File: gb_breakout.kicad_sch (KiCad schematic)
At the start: 19 parts, among them IC1 74ALVC164245DGG_11, IC2 74ALVC164245DGG_11, J1 Conn_02x16_Counter_Clockwise, U1 Cartridge_Bus

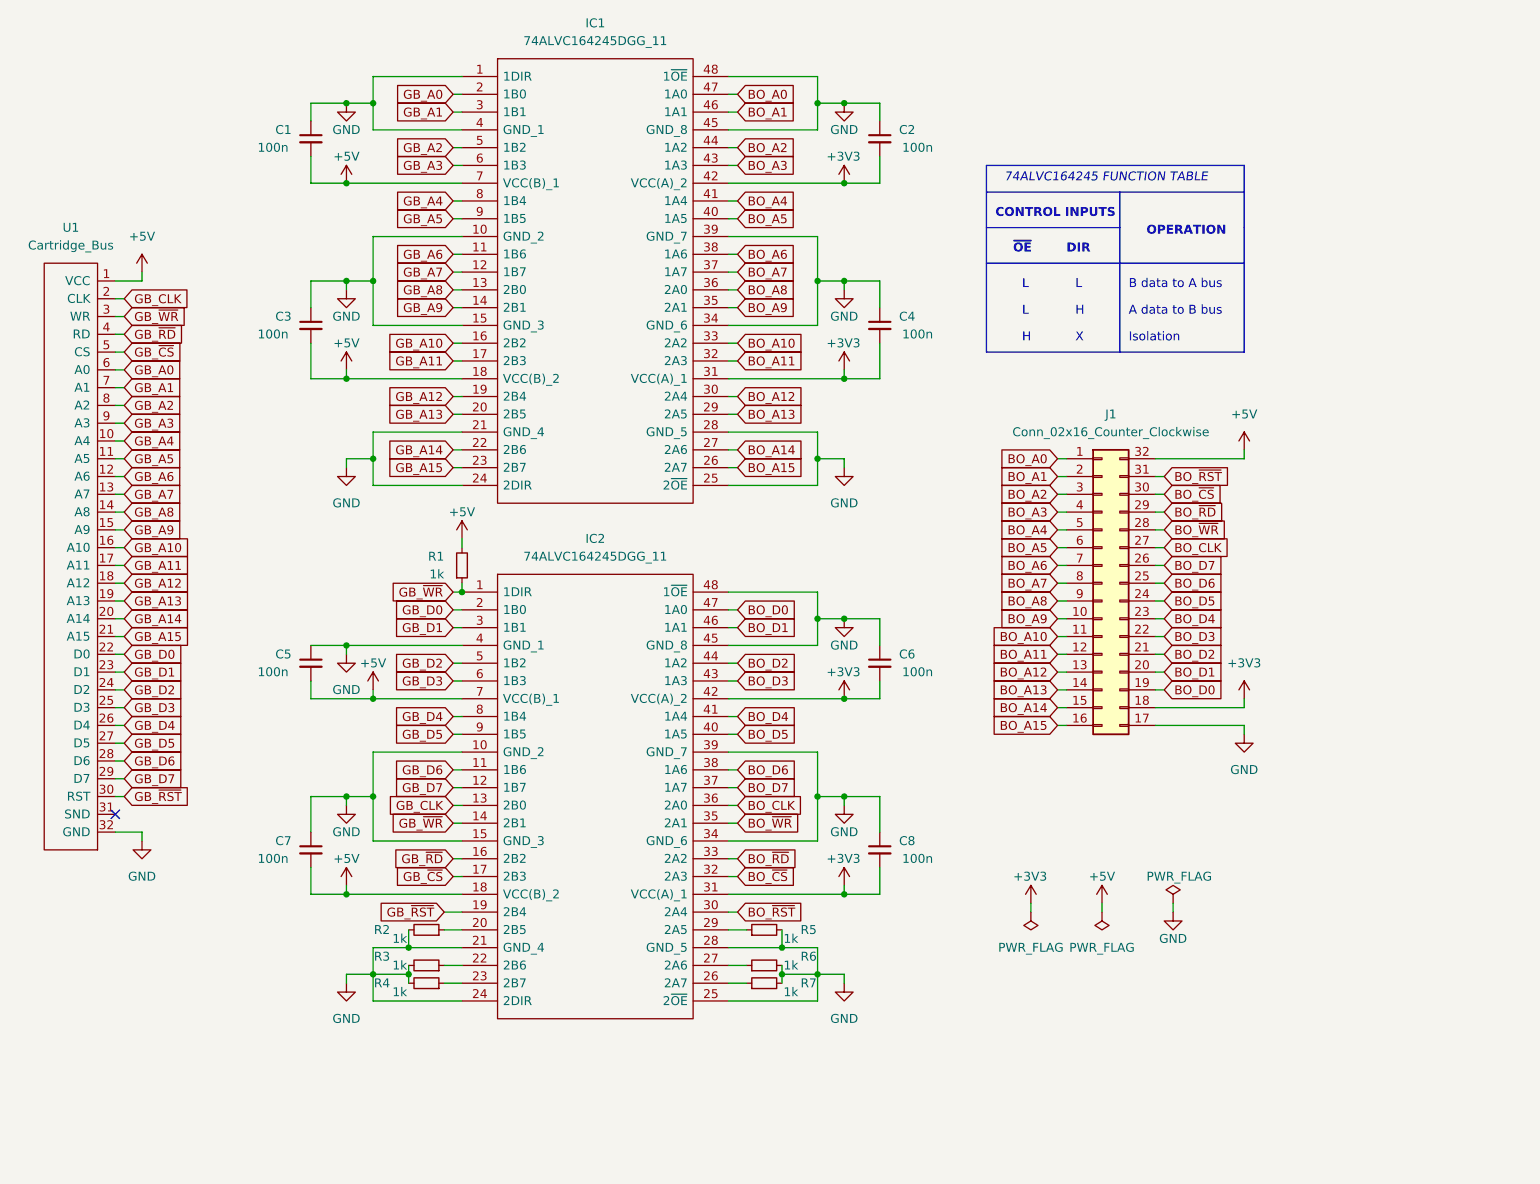
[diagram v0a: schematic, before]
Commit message: replace bus transciever with SN74LVC16T245 to remove power sequencing requirement
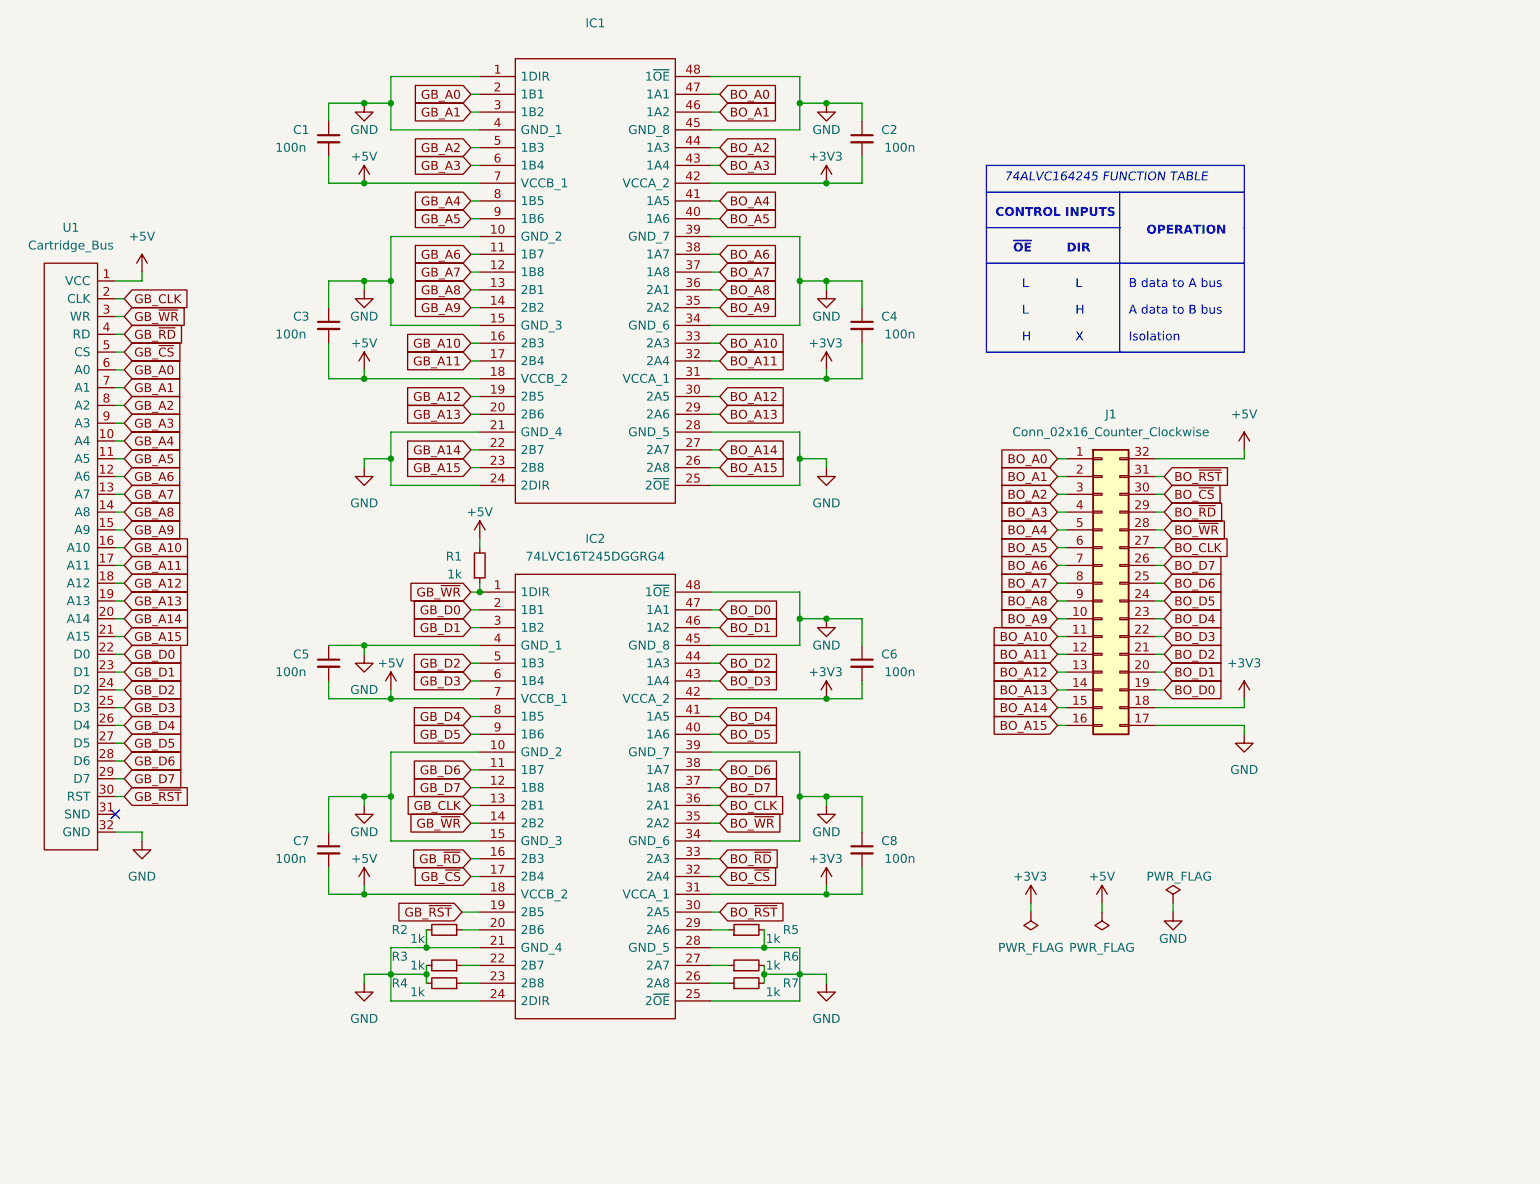
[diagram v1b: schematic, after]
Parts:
- removed IC1, IC2: 74ALVC164245DGG_11, 74ALVC164245DGG_11:SOP50P810X120-48N, symbol 74ALVC164245DGG_11:74ALVC164245DGG_11
- added IC1: (no value), symbol 74LVC16T245DGGRG4:74LVC16T245DGGRG4
- added IC2: 74LVC16T245DGGRG4, symbol 74LVC16T245DGGRG4:74LVC16T245DGGRG4
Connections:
- net +3V3: now also IC1.31 (VCCA_1), IC1.42 (VCCA_2), IC2.31 (VCCA_1), IC2.42 (VCCA_2)
- net +5V: now also IC1.18 (VCCB_2), IC1.7 (VCCB_1), IC2.18 (VCCB_2), IC2.7 (VCCB_1)
- net BO_A0: now also IC1.47 (1A1)
- net BO_A1: now also IC1.46 (1A2)
- net BO_A10: now also IC1.33 (2A3)
- net BO_A11: now also IC1.32 (2A4)
- net BO_A12: now also IC1.30 (2A5)
- net BO_A13: now also IC1.29 (2A6)
- net BO_A14: now also IC1.27 (2A7)
- net BO_A15: now also IC1.26 (2A8)
- net BO_A2: now also IC1.44 (1A3)
- net BO_A3: now also IC1.43 (1A4)
- net BO_A4: now also IC1.41 (1A5)
- net BO_A5: now also IC1.40 (1A6)
- net BO_A6: now also IC1.38 (1A7)
- net BO_A7: now also IC1.37 (1A8)
- net BO_A8: now also IC1.36 (2A1)
- net BO_A9: now also IC1.35 (2A2)
- net BO_CLK: now also IC2.36 (2A1)
- net BO_D0: now also IC2.47 (1A1)
- net BO_D1: now also IC2.46 (1A2)
- net BO_D2: now also IC2.44 (1A3)
- net BO_D3: now also IC2.43 (1A4)
- net BO_D4: now also IC2.41 (1A5)
- net BO_D5: now also IC2.40 (1A6)
- net BO_D6: now also IC2.38 (1A7)
- net BO_D7: now also IC2.37 (1A8)
- net BO_~{CS}: now also IC2.32 (2A4)
- net BO_~{RD}: now also IC2.33 (2A3)
- net BO_~{RST}: now also IC2.30 (2A5)
- net BO_~{WR}: now also IC2.35 (2A2)
- net GB_A0: now also IC1.2 (1B1)
- net GB_A1: now also IC1.3 (1B2)
- net GB_A10: now also IC1.16 (2B3)
- net GB_A11: now also IC1.17 (2B4)
- net GB_A12: now also IC1.19 (2B5)
- net GB_A13: now also IC1.20 (2B6)
- net GB_A14: now also IC1.22 (2B7)
- net GB_A15: now also IC1.23 (2B8)
- net GB_A2: now also IC1.5 (1B3)
- net GB_A3: now also IC1.6 (1B4)
- net GB_A4: now also IC1.8 (1B5)
- net GB_A5: now also IC1.9 (1B6)
- net GB_A6: now also IC1.11 (1B7)
- net GB_A7: now also IC1.12 (1B8)
- net GB_A8: now also IC1.13 (2B1)
- net GB_A9: now also IC1.14 (2B2)
- net GB_CLK: now also IC2.13 (2B1)
- net GB_D0: now also IC2.2 (1B1)
- net GB_D1: now also IC2.3 (1B2)
- net GB_D2: now also IC2.5 (1B3)
- net GB_D3: now also IC2.6 (1B4)
- net GB_D4: now also IC2.8 (1B5)
- net GB_D5: now also IC2.9 (1B6)
- net GB_D6: now also IC2.11 (1B7)
- net GB_D7: now also IC2.12 (1B8)
- net GB_~{CS}: now also IC2.17 (2B4)
- net GB_~{RD}: now also IC2.16 (2B3)
- net GB_~{RST}: now also IC2.19 (2B5)
- net GB_~{WR}: now also IC2.1 (1DIR), IC2.14 (2B2)
- net GND: now also IC1.1 (1DIR), IC1.10 (GND_2), IC1.15 (GND_3), IC1.21 (GND_4), IC1.24 (2DIR), IC1.25 (2~{OE}), IC1.28 (GND_5), IC1.34 (GND_6), IC1.39 (GND_7), IC1.4 (GND_1), IC1.45 (GND_8), IC1.48 (1~{OE}), IC2.10 (GND_2), IC2.15 (GND_3), IC2.21 (GND_4), IC2.24 (2DIR), IC2.25 (2~{OE}), IC2.28 (GND_5), IC2.34 (GND_6), IC2.39 (GND_7), IC2.4 (GND_1), IC2.45 (GND_8), IC2.48 (1~{OE})
- net at R3.1: now also IC2.22 (2B7)
- net at R7.1: now also IC2.26 (2A8)
- net at R2.1: now also IC2.20 (2B6)
- net at R4.1: now also IC2.23 (2B8)
- net at R6.1: now also IC2.27 (2A7)
- net at R5.1: now also IC2.29 (2A6)
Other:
- moved on the sheet: C1, C2, C3, C4, C5, C6, C7, C8, R1, R2, R3, R4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

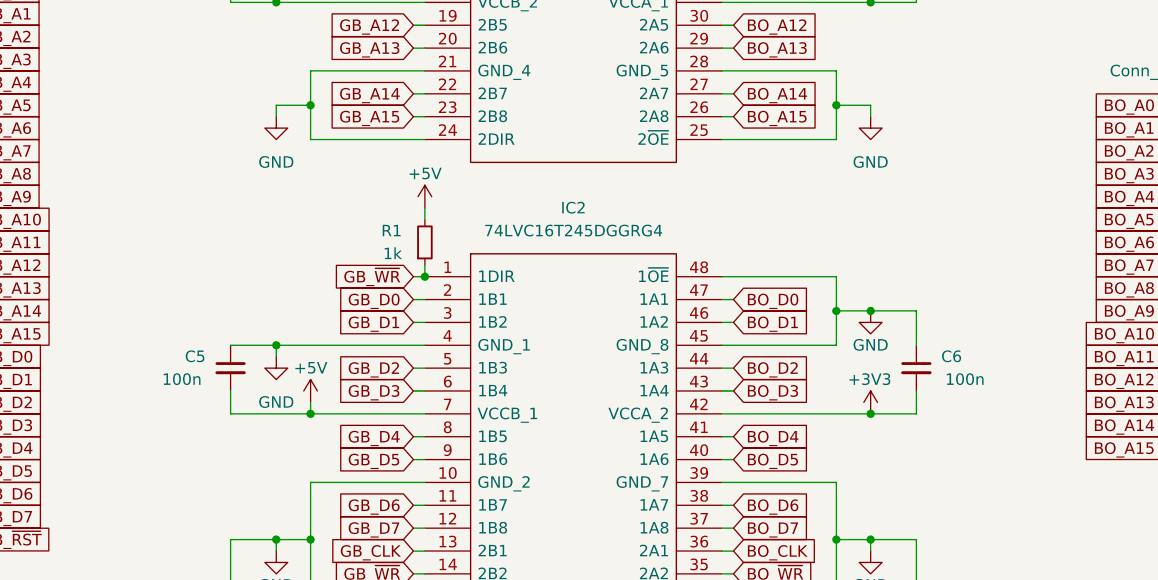
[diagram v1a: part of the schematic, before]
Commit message: OE on 2nd bus transciever now connected to A15, isolates data bus from the cartridge when GB is not accessing the cartridge specifically (ROM reads only at the moment)
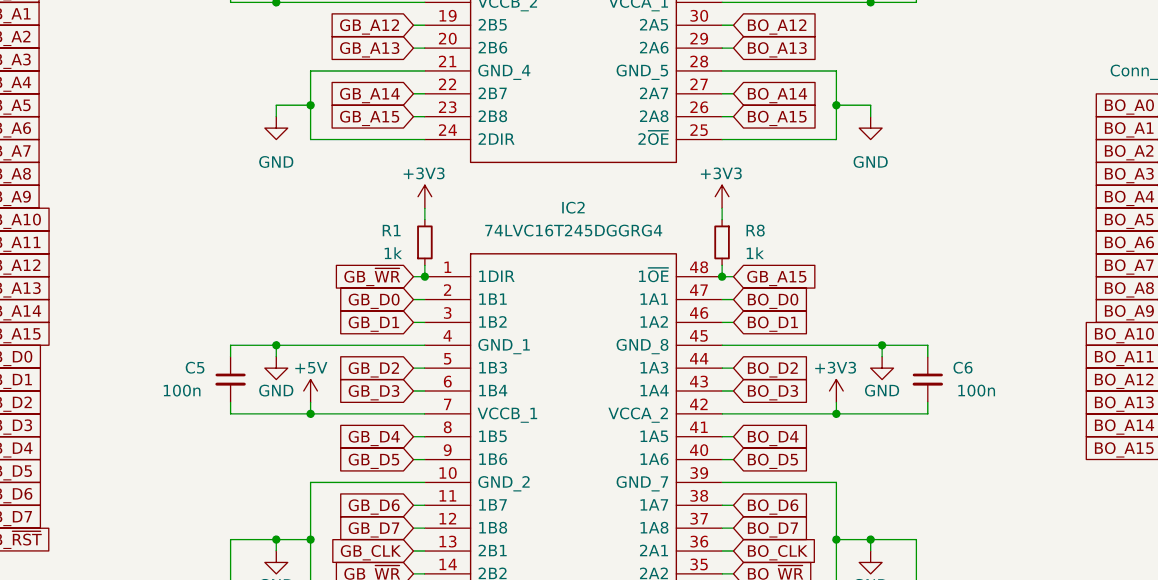
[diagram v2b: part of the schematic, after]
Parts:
- added R8: 1k, Resistor_SMD:R_0402_1005Metric, symbol Device:R_Small
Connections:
- net +3V3: now also R1.2, R8.1
- net +5V: no longer R1.2
- net GB_A15: now also IC2.48 (1~{OE}), R8.2
- net GND: no longer IC2.48 (1~{OE})
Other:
- moved on the sheet: C5, C6

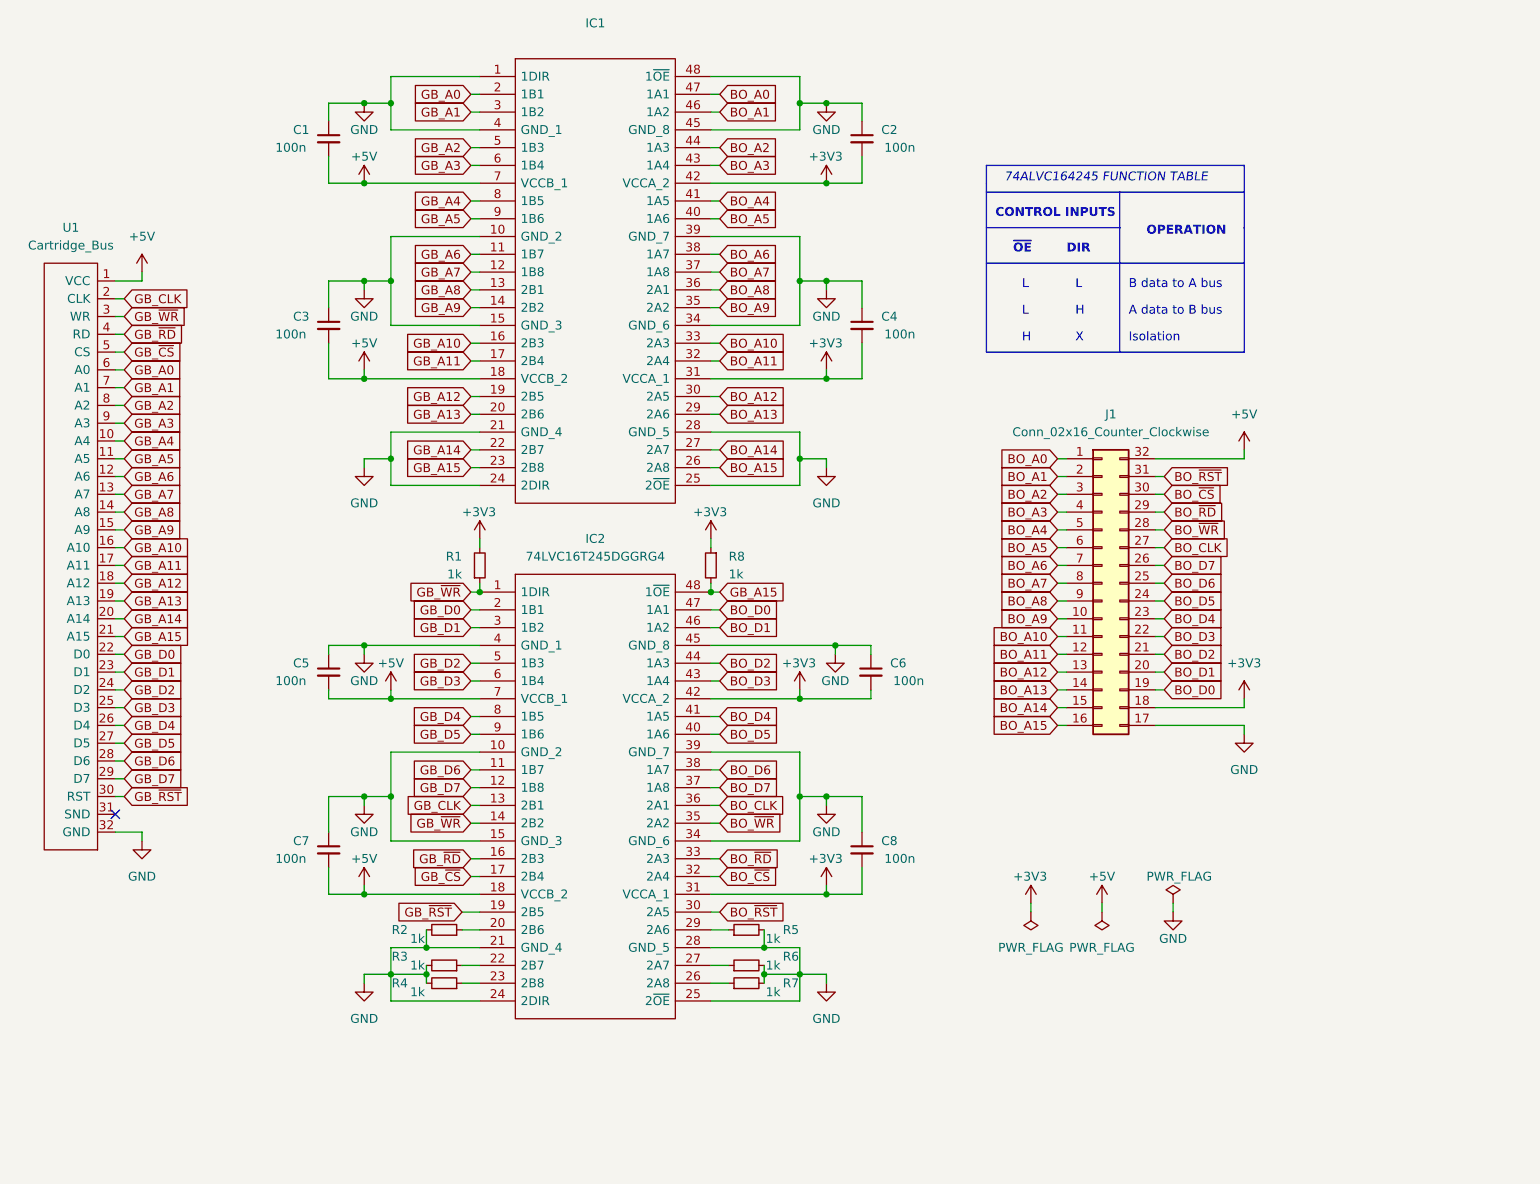
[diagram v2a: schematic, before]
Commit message: fixed reset line direction in schematic by adding a dedicated bus transciever
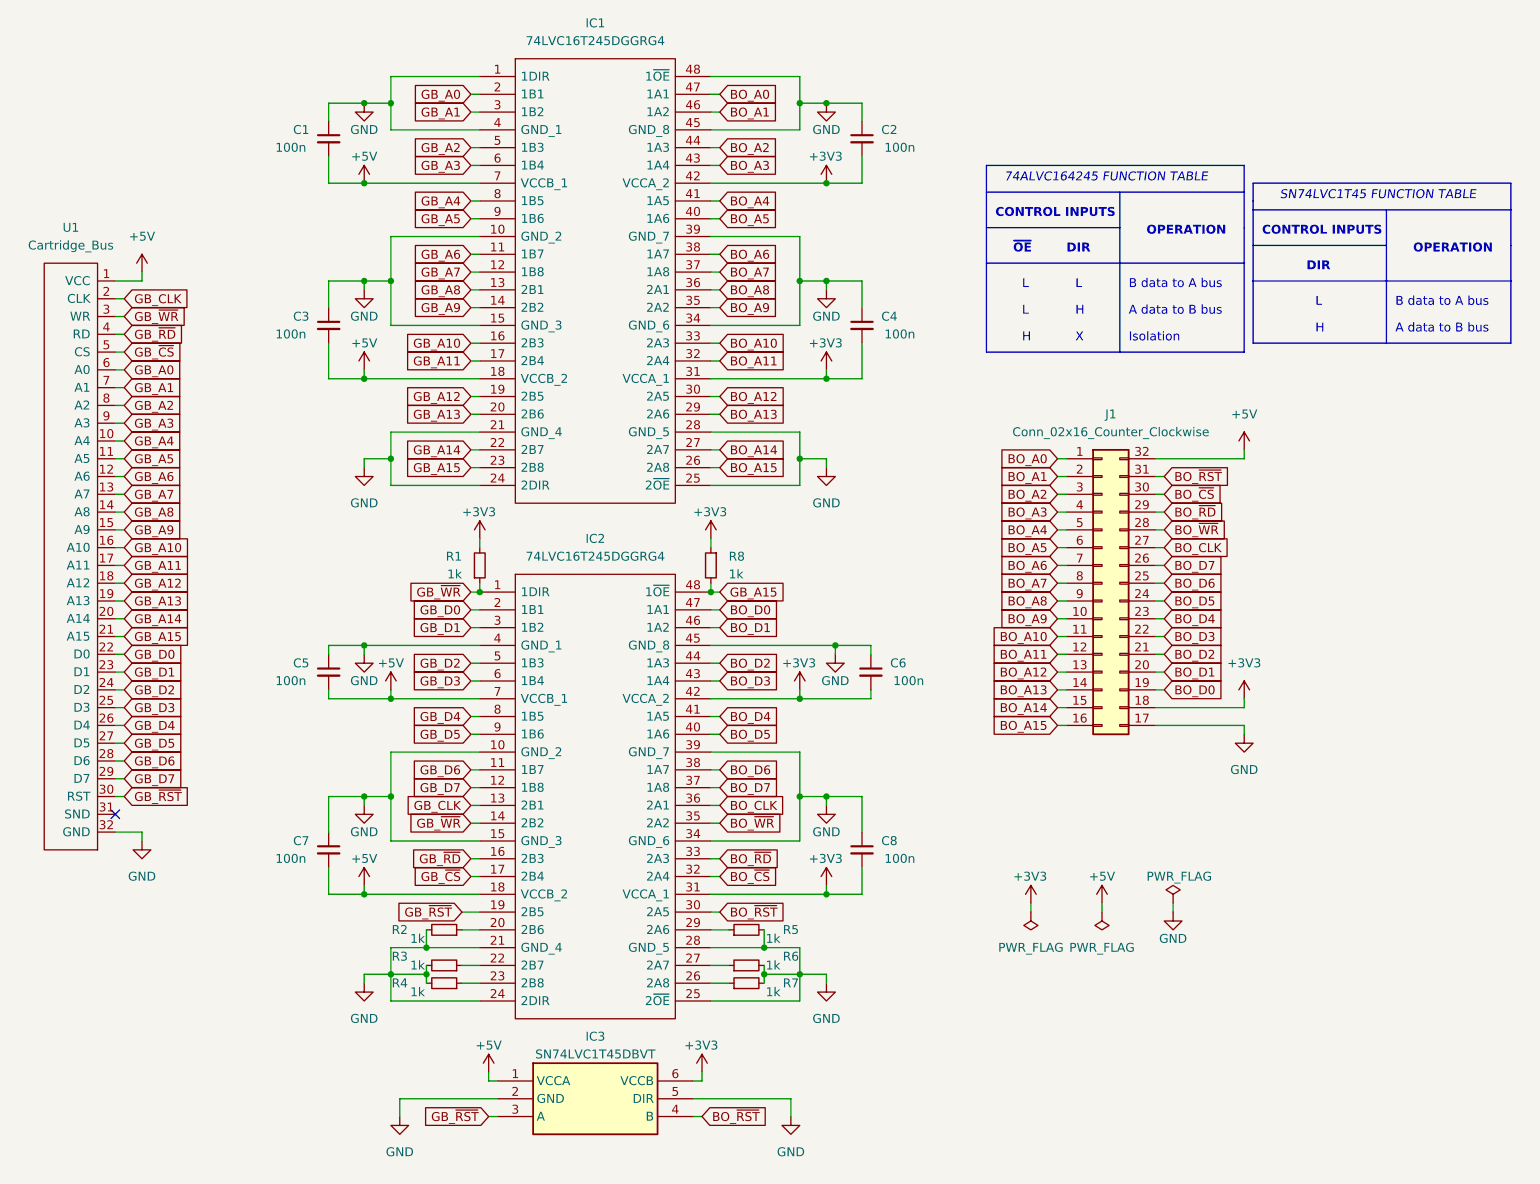
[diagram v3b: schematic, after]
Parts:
- added IC3: SN74LVC1T45DBVT, SOT95P280X145-6N, symbol SN74LVC1T45DBVT:SN74LVC1T45DBVT
- IC1: value (none) -> 74LVC16T245DGGRG4; footprint (none) -> 74LVC16T245DGGRG4:SOP50P810X120-48N
- IC2: footprint (none) -> 74LVC16T245DGGRG4:SOP50P810X120-48N
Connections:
- net +3V3: now also IC3.6 (VCCB)
- net +5V: now also IC3.1 (VCCA)
- net BO_~{RST}: now also IC3.4 (B)
- net GB_~{RST}: now also IC3.3 (A)
- net GND: now also IC3.2 (GND), IC3.5 (DIR)
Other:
- note added: "SN74LVC1T45 FUNCTION TABLE"

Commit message: disconnect reset signal from IC2
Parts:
- IC3: footprint SOT95P280X145-6N -> SN74LVC1T45DBVT:SOT95P280X145-6N
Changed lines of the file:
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@@
   (symbol (lib_id "power:+3V3") (at 165.1 111.76 0) (unit 1)
     (in_bom yes) (on_board yes) (dnp no)
-    (property "Reference" "#PWR?" (at 165.1 115.57 0)
+    (property "Reference" "#PWR0109" (at 165.1 115.57 0)
       (effects (font (size 1.27 1.27)) hide)
     )
@@
       (project "gb_breakout"
         (path "/e63e39d7-6ac0-4ffd-8aa3-1841a4541b55"
-          (reference "#PWR?") (unit 1)
+          (reference "#PWR0109") (unit 1)
         )
       )
@@
       (effects (font (size 1.27 1.27)))
     )
-    (property "Footprint" "SOT95P280X145-6N" (at 146.05 262.56 0)
+    (property "Footprint" "SN74LVC1T45DBVT:SOT95P280X145-6N" (at 146.05 262.56 0)
       (effects (font (size 1.27 1.27)) (justify left top) hide)
     )
